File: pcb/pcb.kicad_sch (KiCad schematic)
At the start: 50 parts, among them J1 USB_C_Receptacle_USB2.0_14P, J2 VG6328A, J3 LCD, J4 Debug, J5 Moisture, J6 Logs, J8 LCD CTRL, SW1 PWR SWITCH, U1 TLV62569DBV, U2 STM32F446RETx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

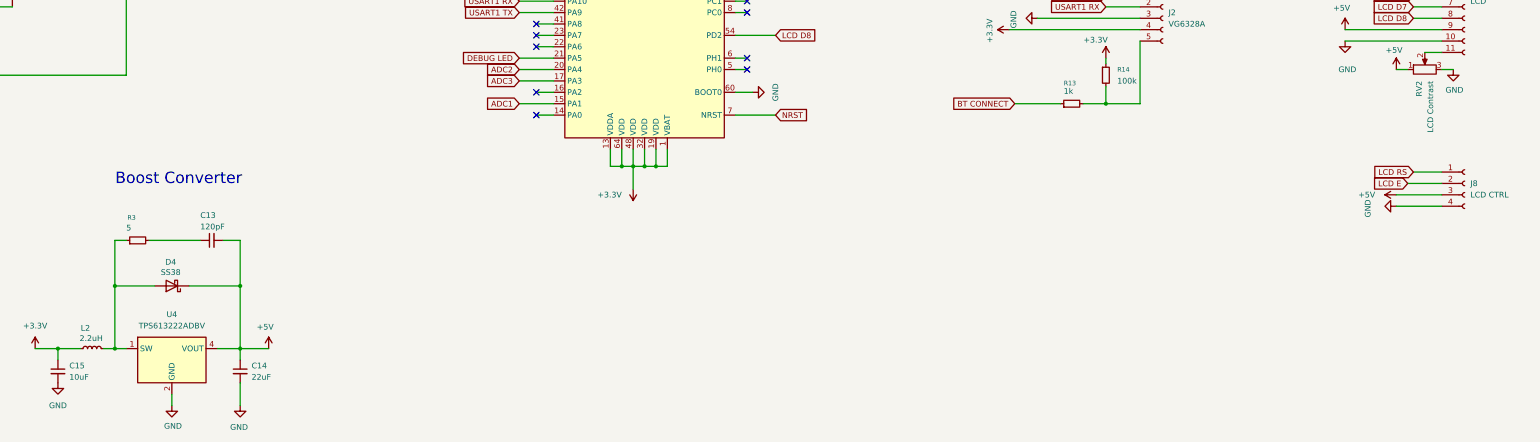
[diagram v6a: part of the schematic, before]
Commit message: fix incorrect labels on schematic
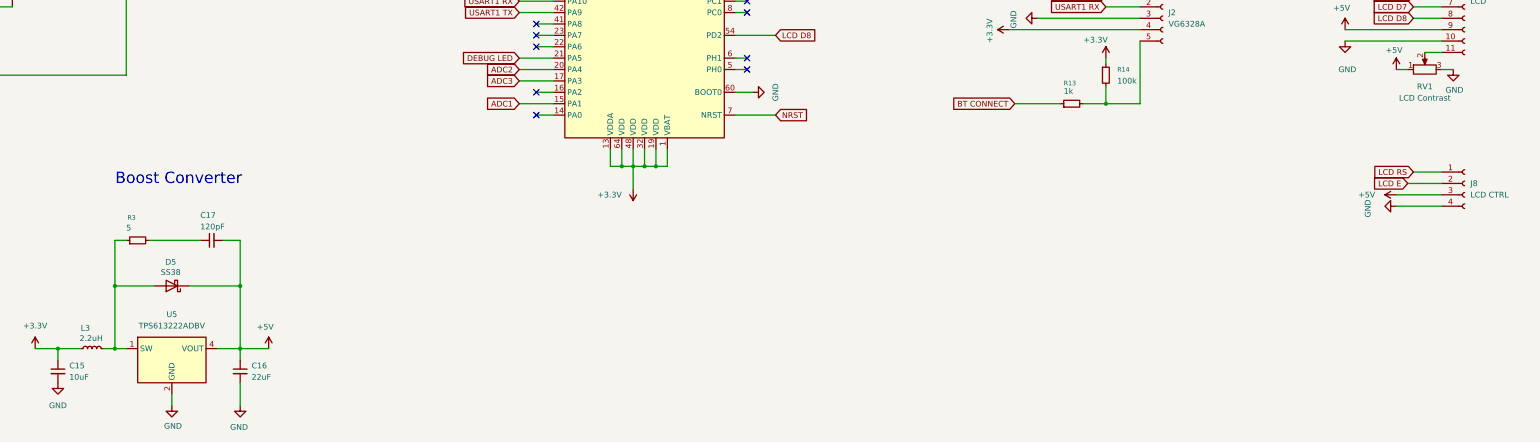
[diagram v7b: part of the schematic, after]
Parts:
- renumbered C14 to C16, C13 to C17, D4 to D5, L2 to L3, RV2 to RV1, U4 to U5
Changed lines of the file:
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@@
 		(dnp no)
 		(fields_autoplaced yes)
-		(property "Reference" "RV2"
-			(at 370.8399 180.34 0)
+		(property "Reference" "RV1"
+			(at 372.11 181.61 90)
 			(effects
 				(font
 					(size 1.27 1.27)
 				)
-				(justify right)
 			)
 		)
 		(property "Value" "LCD Contrast"
-			(at 373.3799 180.34 0)
+			(at 372.11 184.15 90)
 			(effects
 				(font
 					(size 1.27 1.27)
 				)
-				(justify right)
 			)
 		)
@@
 			(project "pcb"
 				(path "/a02550bc-85b4-480d-868d-ccdfd0f6046d"
-					(reference "RV2")
+					(reference "RV1")
 					(unit 1)
 				)
@@
 		(dnp no)
 		(fields_autoplaced yes)
-		(property "Reference" "U4"
+		(property "Reference" "U5"
 			(at 92.71 232.41 0)
 			(effects
@@
 			(project "pcb"
 				(path "/a02550bc-85b4-480d-868d-ccdfd0f6046d"
-					(reference "U4")
+					(reference "U5")
 					(unit 1)
 				)
@@
 		(on_board yes)
 		(dnp no)
-		(property "Reference" "C13"
+		(property "Reference" "C17"
 			(at 99.06 210.312 90)
 			(effects
@@
 			(project "pcb"
 				(path "/a02550bc-85b4-480d-868d-ccdfd0f6046d"
-					(reference "C13")
+					(reference "C17")
 					(unit 1)
 				)
@@
 		(on_board yes)
 		(dnp no)
-		(property "Reference" "L2"
+		(property "Reference" "L3"
 			(at 72.39 235.458 90)
 			(effects
@@
 			(project "pcb"
 				(path "/a02550bc-85b4-480d-868d-ccdfd0f6046d"
-					(reference "L2")
+					(reference "L3")
 					(unit 1)
 				)
@@
 		(on_board yes)
 		(dnp no)
-		(property "Reference" "D4"
+		(property "Reference" "D5"
 			(at 92.456 220.726 0)
 			(effects
@@
 			(project "pcb"
 				(path "/a02550bc-85b4-480d-868d-ccdfd0f6046d"
-					(reference "D4")
+					(reference "D5")
 					(unit 1)
 				)
@@
 		(dnp no)
 		(fields_autoplaced yes)
-		(property "Reference" "C14"
+		(property "Reference" "C16"
 			(at 110.49 243.8462 0)
 			(effects
@@
 			(project "pcb"
 				(path "/a02550bc-85b4-480d-868d-ccdfd0f6046d"
-					(reference "C14")
+					(reference "C16")
 					(unit 1)
 				)

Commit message: change schematic name
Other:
- title: Plant Monitor PCB -> planted-pro main board
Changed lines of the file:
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@@
 	(paper "A3")
 	(title_block
-		(title "Plant Monitor PCB")
-		(rev "1")
+		(title "planted-pro main board")
+		(rev "4")
 	)
 	(text "Battery Monitor"
